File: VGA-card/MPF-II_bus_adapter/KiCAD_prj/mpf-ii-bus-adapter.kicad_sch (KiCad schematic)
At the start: 2 parts, among them J1 Bus_Apple_II_Card_Side, J2 Bus_Apple_II_Computer_Side

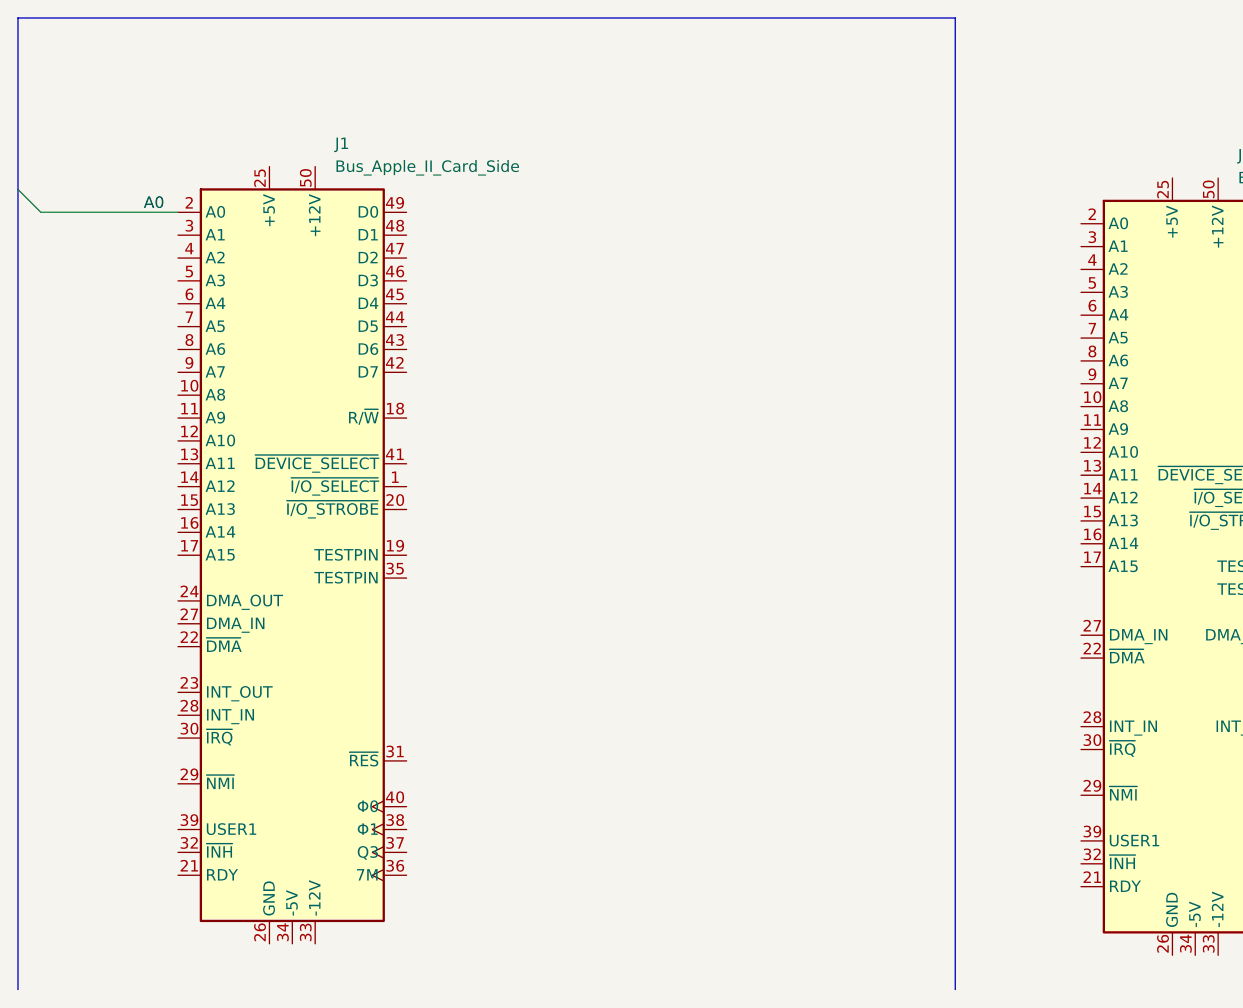
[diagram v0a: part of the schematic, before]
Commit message: [Bus-adapter] Address bus added to schematics
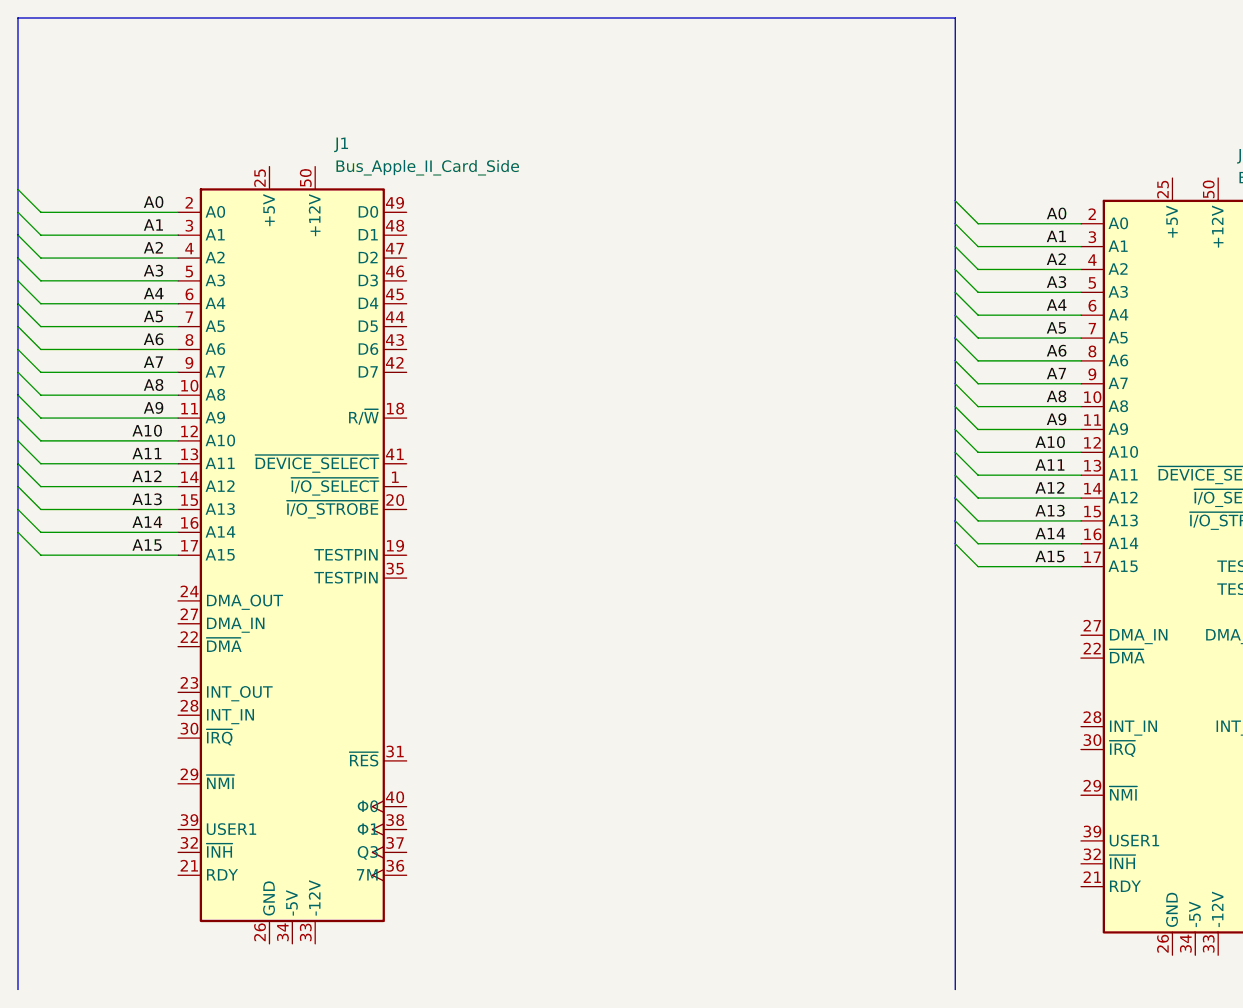
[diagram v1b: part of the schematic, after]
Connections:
- net A0: now also J2.2 (A0)
- net A8: now reaches J2.10 (A8)
- net A8: now also J1.10 (A8)
- net A9: now reaches J2.11 (A9)
- net A9: now also J1.11 (A9)
- net A10: now reaches J2.12 (A10)
- net A10: now also J1.12 (A10)
- net A11: now reaches J2.13 (A11)
- net A11: now also J1.13 (A11)
- net A12: now reaches J2.14 (A12)
- net A12: now also J1.14 (A12)
- net A13: now reaches J2.15 (A13)
- net A13: now also J1.15 (A13)
- net A14: now reaches J2.16 (A14)
- net A14: now also J1.16 (A14)
- net A15: now reaches J2.17 (A15)
- net A15: now also J1.17 (A15)
- net A1: now reaches J2.3 (A1)
- net A1: now also J1.3 (A1)
- net A2: now reaches J2.4 (A2)
- net A2: now also J1.4 (A2)
- net A3: now reaches J2.5 (A3)
- net A3: now also J1.5 (A3)
- net A4: now reaches J2.6 (A4)
- net A4: now also J1.6 (A4)
- net A5: now reaches J2.7 (A5)
- net A5: now also J1.7 (A5)
- net A6: now reaches J2.8 (A6)
- net A6: now also J1.8 (A6)
- net A7: now reaches J2.9 (A7)
- net A7: now also J1.9 (A7)

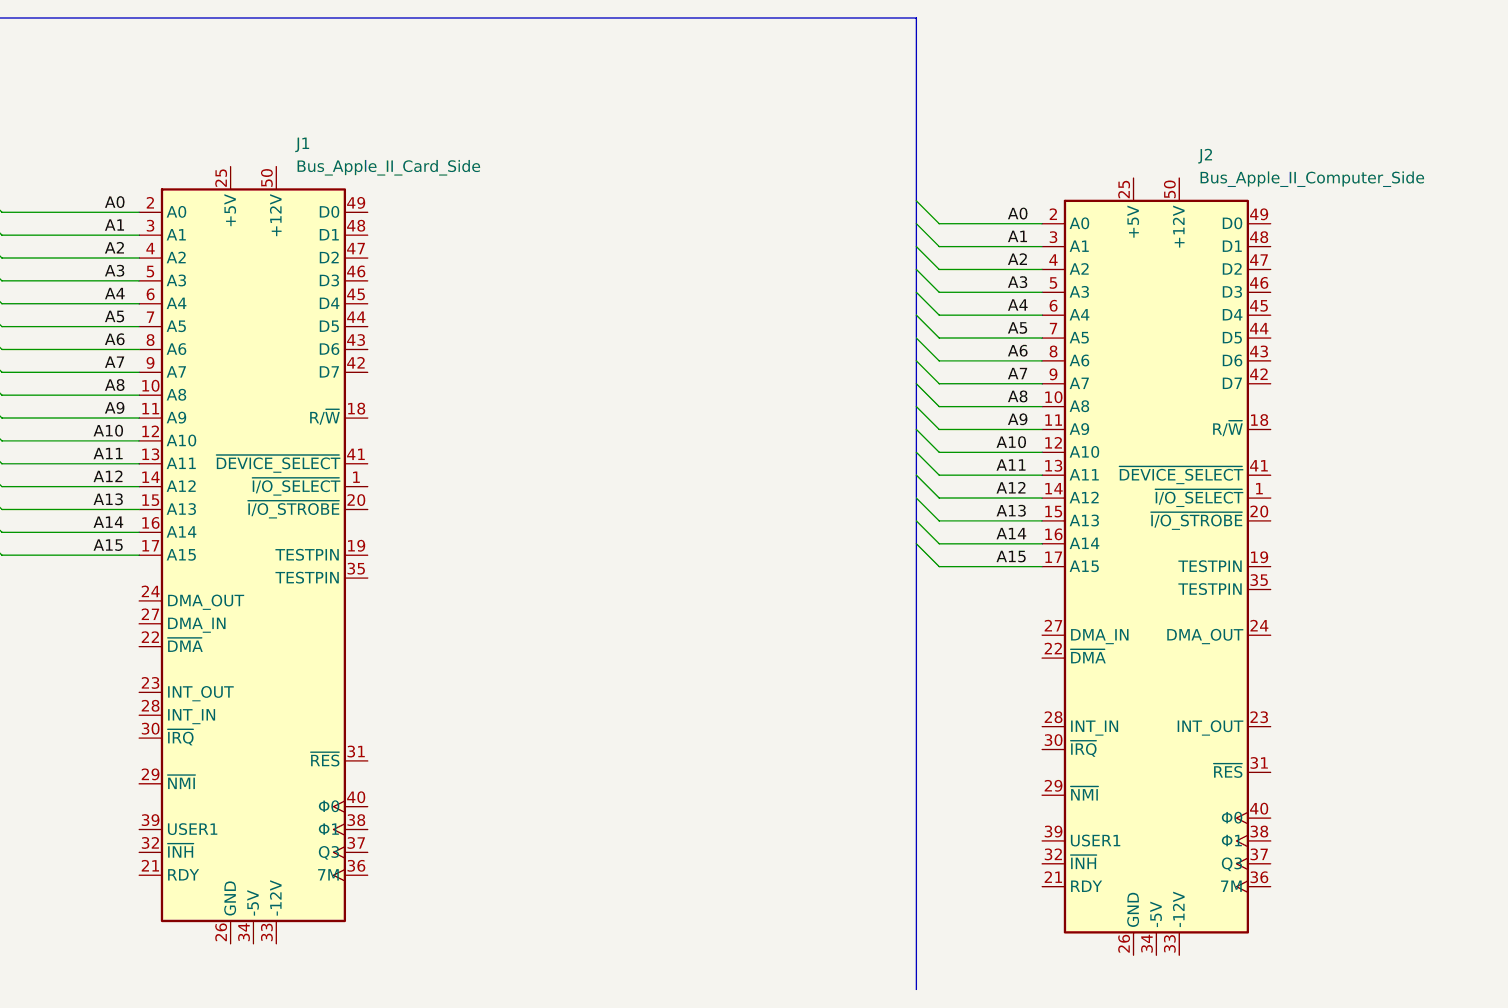
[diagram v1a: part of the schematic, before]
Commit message: Data bus added
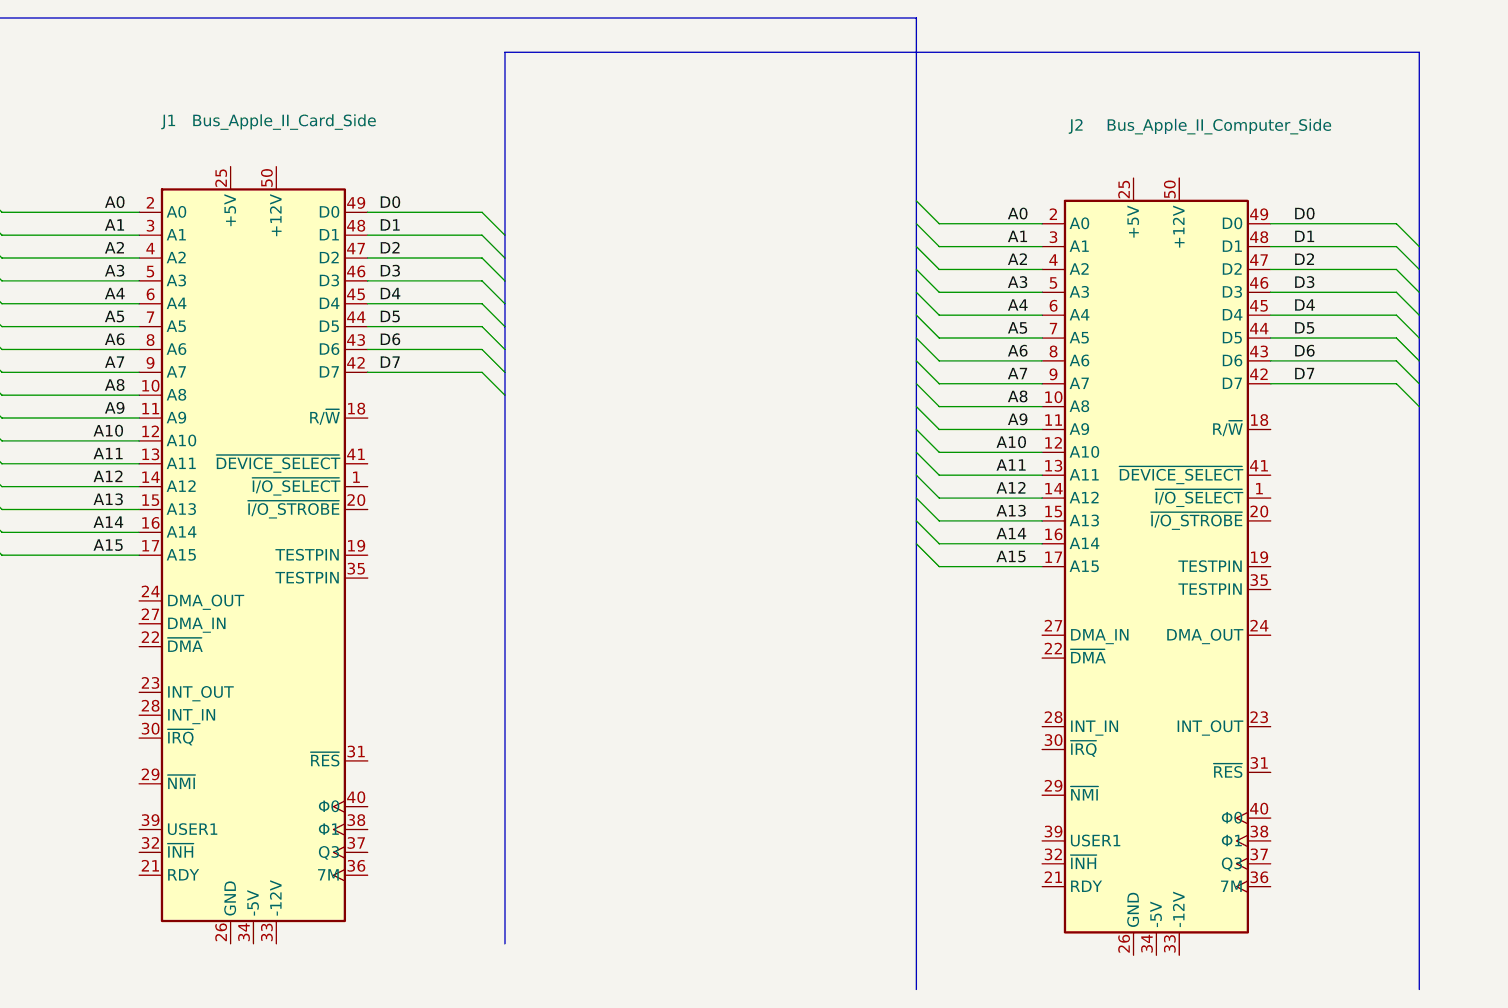
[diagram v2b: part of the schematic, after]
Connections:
- net D7: now reaches J2.42 (D7)
- net D7: now also J1.42 (D7)
- net D6: now reaches J2.43 (D6)
- net D6: now also J1.43 (D6)
- net D5: now reaches J2.44 (D5)
- net D5: now also J1.44 (D5)
- net D4: now reaches J2.45 (D4)
- net D4: now also J1.45 (D4)
- net D3: now reaches J2.46 (D3)
- net D3: now also J1.46 (D3)
- net D2: now reaches J2.47 (D2)
- net D2: now also J1.47 (D2)
- net D1: now reaches J2.48 (D1)
- net D1: now also J1.48 (D1)
- net D0: now reaches J2.49 (D0)
- net D0: now also J1.49 (D0)

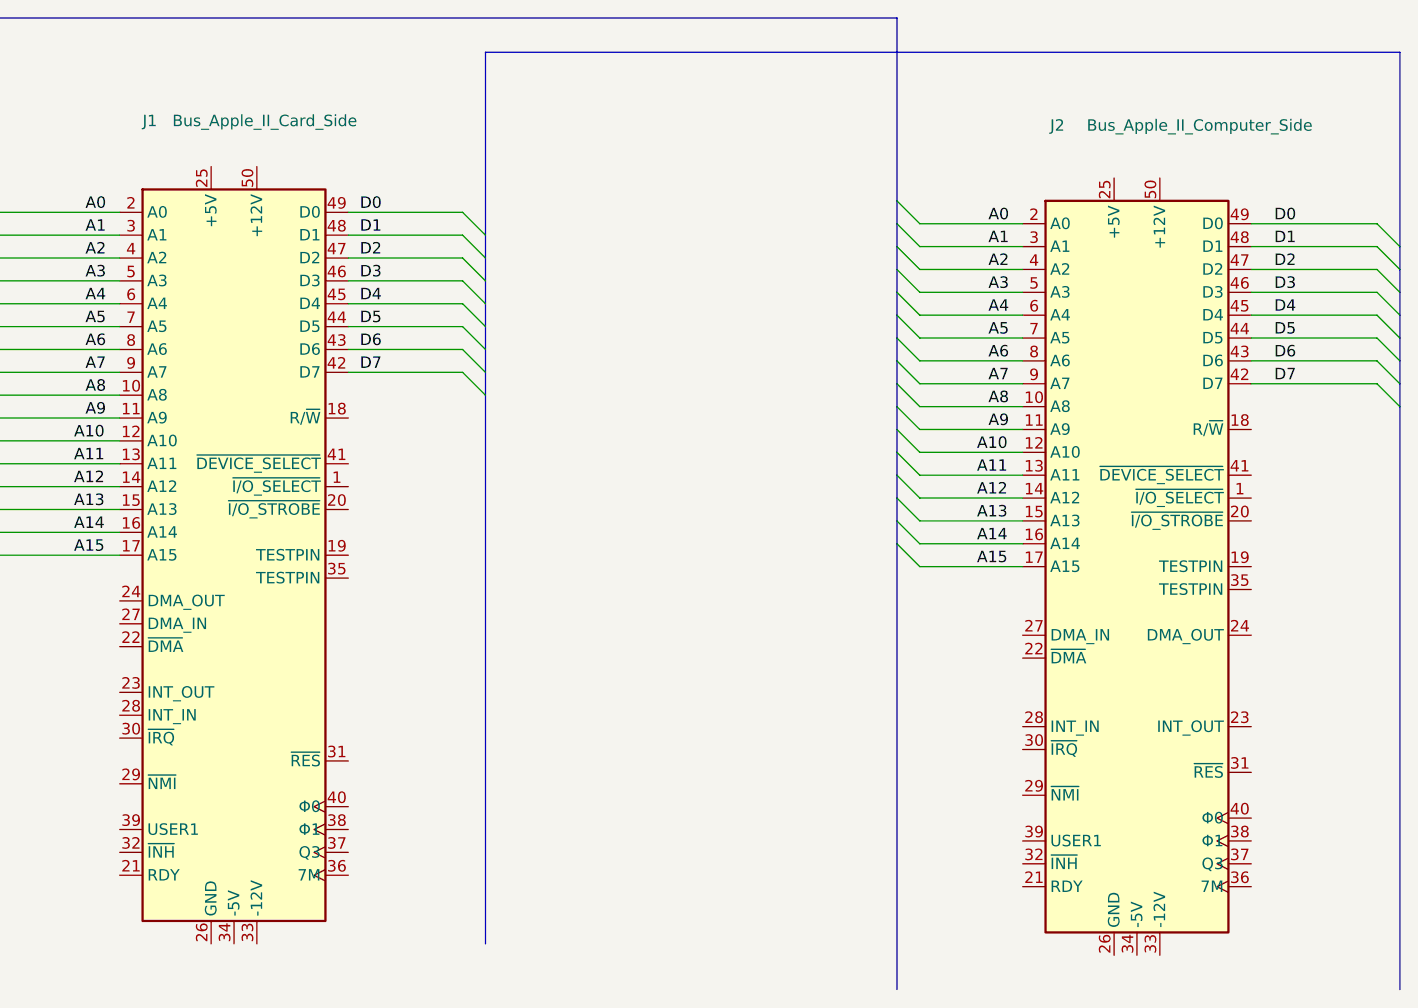
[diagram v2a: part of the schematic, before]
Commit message: DEVSEL and RW are added
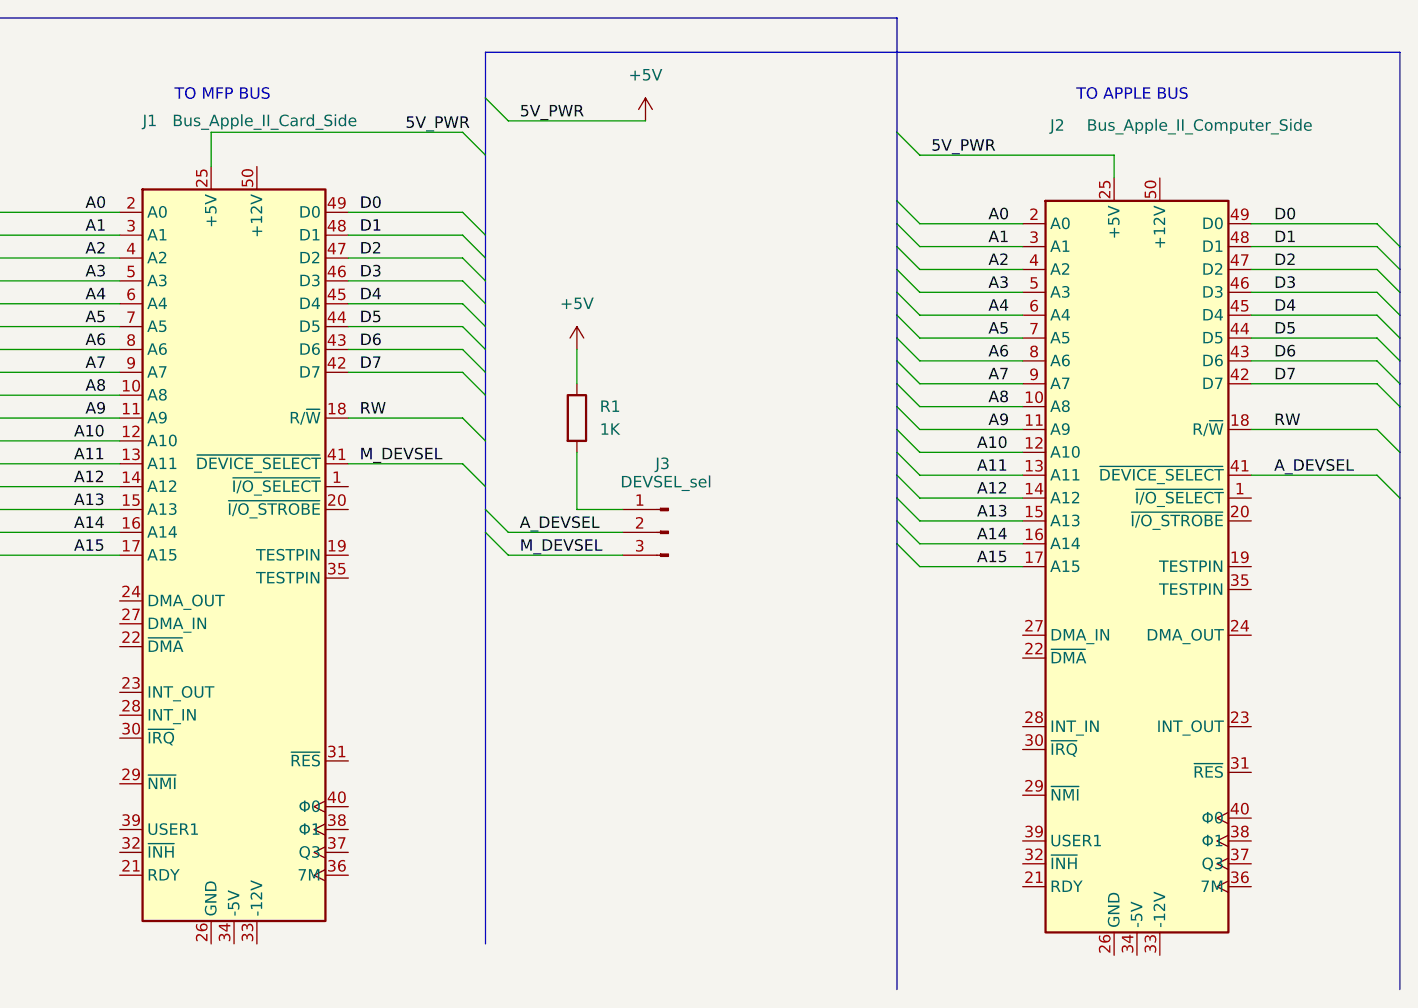
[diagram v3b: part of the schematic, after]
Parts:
- added J3: DEVSEL_sel, Connector_PinHeader_2.54mm:PinHeader_1x03_P2.54mm_Vertical, symbol Connector:Conn_01x03_Pin
- added R1: 1K, Resistor_THT:R_Axial_DIN0207_L6.3mm_D2.5mm_P10.16mm_Horizontal, symbol Device:R
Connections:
- net RW: now reaches J2.18 (R/~{W})
- net RW: now also J1.18 (R/~{W})
- net +5V: now reaches J2.25 (+5V)
- net +5V: now also J1.25 (+5V), R1.1
- net A_DEVSEL: now reaches J2.41 (~{DEVICE_SELECT})
- net A_DEVSEL: now also J3.2 (Pin_2)
- net M_DEVSEL: now reaches J1.41 (~{DEVICE_SELECT})
- net M_DEVSEL: now also J3.3 (Pin_3)
- new net: J3.1 (Pin_1), R1.2
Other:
- note added: "TO APPLE BUS"
- note added: "TO MFP BUS"
